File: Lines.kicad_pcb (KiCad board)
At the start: 2 copper layers, 29.5 x 100 mm, 0 parts

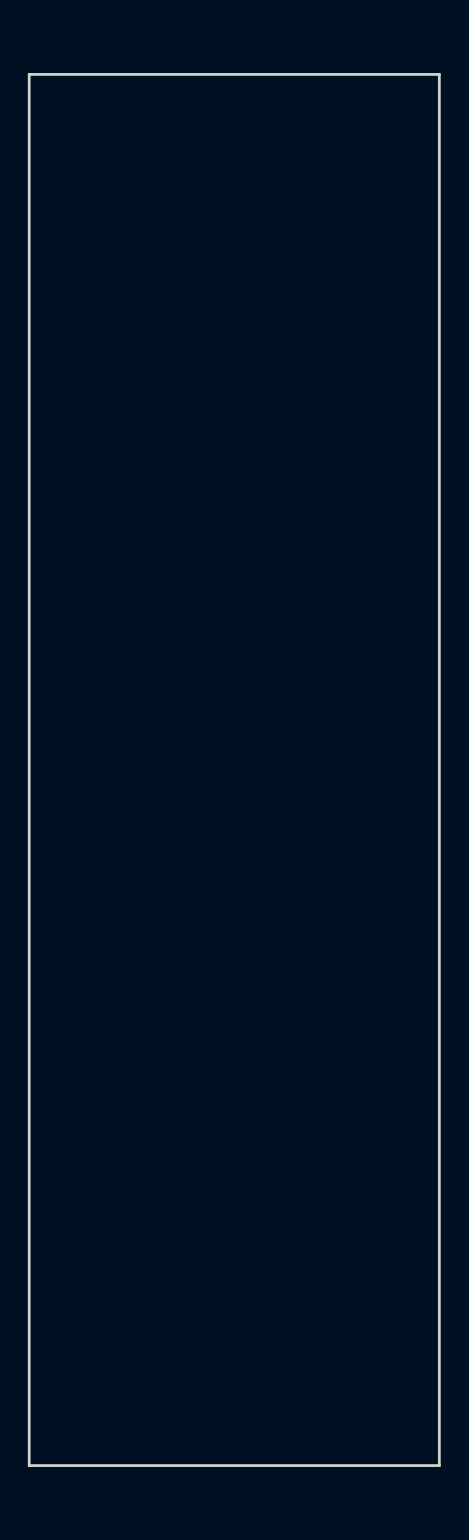
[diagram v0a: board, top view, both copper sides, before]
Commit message: Corrected board dimensions and added jacks.
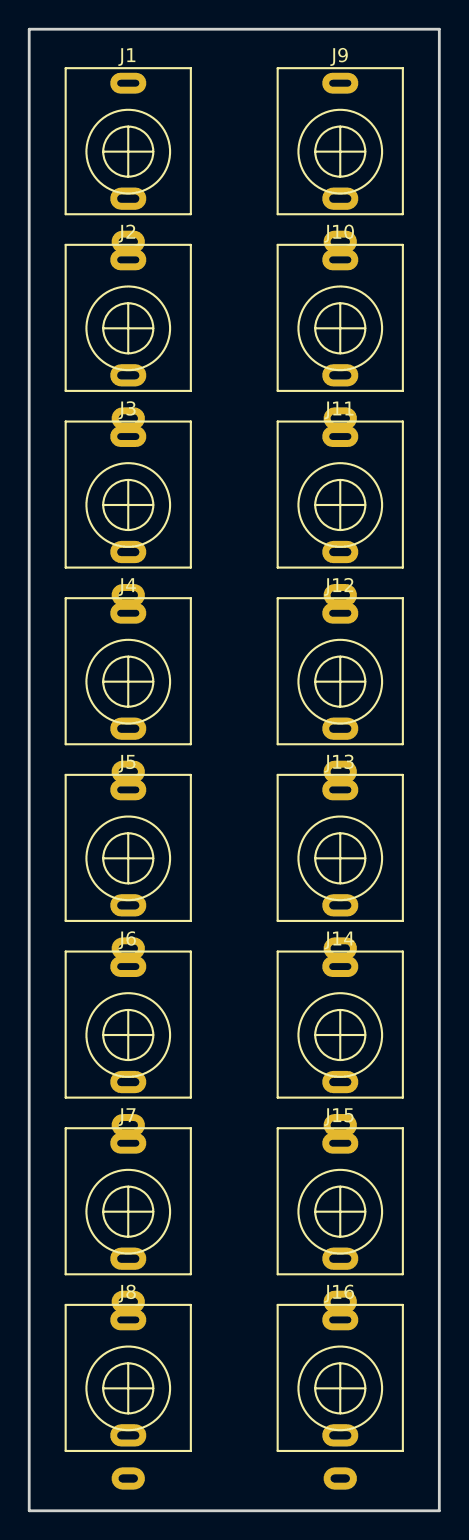
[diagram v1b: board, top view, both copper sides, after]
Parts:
- added J1: AudioJack2_SwitchT, Local:PJ398SM, F.Cu at (119.4, 57.1)
- added J10: AudioJack2_SwitchT, Local:PJ398SM, F.Cu at (134.6, 69.8)
- added J11: AudioJack2_SwitchT, Local:PJ398SM, F.Cu at (134.6, 82.5)
- added J12: AudioJack2_SwitchT, Local:PJ398SM, F.Cu at (134.6, 95.2)
- added J13: AudioJack2_SwitchT, Local:PJ398SM, F.Cu at (134.6, 108.0)
- added J14: AudioJack2_SwitchT, Local:PJ398SM, F.Cu at (134.6, 120.7)
- added J15: AudioJack2_SwitchT, Local:PJ398SM, F.Cu at (134.6, 133.3)
- added J16: AudioJack2_SwitchT, Local:PJ398SM, F.Cu at (134.6, 146.1)
- added J2: AudioJack2_SwitchT, Local:PJ398SM, F.Cu at (119.4, 69.8)
- added J3: AudioJack2_SwitchT, Local:PJ398SM, F.Cu at (119.4, 82.5)
- added J4: AudioJack2_SwitchT, Local:PJ398SM, F.Cu at (119.4, 95.2)
- added J5: AudioJack2_SwitchT, Local:PJ398SM, F.Cu at (119.4, 108.0)
- added J6: AudioJack2_SwitchT, Local:PJ398SM, F.Cu at (119.4, 120.7)
- added J7: AudioJack2_SwitchT, Local:PJ398SM, F.Cu at (119.4, 133.3)
- added J8: AudioJack2_SwitchT, Local:PJ398SM, F.Cu at (119.4, 146.1)
- added J9: AudioJack2_SwitchT, Local:PJ398SM, F.Cu at (134.6, 57.1)
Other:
- board size 29.5 x 100 mm -> 29.5 x 106.5 mm

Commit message: Complete placement.
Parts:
- added C1: 220p, Capacitor_SMD:C_0603_1608Metric, B.Cu at (125.0, 86.2)
- added C10: 100n, Capacitor_SMD:C_0603_1608Metric, B.Cu at (122.0, 133.3)
- added C11: 220p, Capacitor_SMD:C_0603_1608Metric, B.Cu at (129.2, 142.4)
- added C12: 220p, Capacitor_SMD:C_0603_1608Metric, B.Cu at (125.0, 142.4)
- added C13: 22u, Capacitor_SMD:CP_Elec_5x5.4, B.Cu at (119.4, 70.6)
- added C14: 22u, Capacitor_SMD:CP_Elec_5x5.4, B.Cu at (134.9, 70.6)
- added C2: 220p, Capacitor_SMD:C_0603_1608Metric, B.Cu at (129.2, 86.2)
- added C3: 100n, Capacitor_SMD:C_0603_1608Metric, B.Cu at (122.0, 95.2)
- added C4: 100n, Capacitor_SMD:C_0603_1608Metric, B.Cu at (132.0, 95.2)
- added C5: 220p, Capacitor_SMD:C_0603_1608Metric, B.Cu at (129.2, 104.3)
- added C6: 220p, Capacitor_SMD:C_0603_1608Metric, B.Cu at (125.0, 104.3)
- added C7: 220p, Capacitor_SMD:C_0603_1608Metric, B.Cu at (125.0, 124.3)
- added C8: 220p, Capacitor_SMD:C_0603_1608Metric, B.Cu at (129.2, 124.3)
- added C9: 100n, Capacitor_SMD:C_0603_1608Metric, B.Cu at (132.0, 133.3)
- added D1: DFLR1400-7, Diode_SMD:D_PowerDI-123, B.Cu at (115.4, 59.8)
- added D2: DFLR1400-7, Diode_SMD:D_PowerDI-123, B.Cu at (138.8, 59.8)
- added D3: LED, LED_SMD:LED_0603_1608Metric_Castellated, B.Cu at (115.4, 52.8)
- added FB1: Ferrite_Bead, Inductor_SMD:L_0603_1608Metric, B.Cu at (115.4, 65.0)
- added FB2: Ferrite_Bead, Inductor_SMD:L_0603_1608Metric, B.Cu at (138.8, 65.0)
- added J17: Conn_02x05_Odd_Even, Connector_PinHeader_2.54mm:PinHeader_2x05_P2.54mm_Vertical, B.Cu at (125.7, 62.6)
- added R1: 100k, Resistor_SMD:R_0603_1608Metric, B.Cu at (119.4, 56.3)
- added R10: 680, Resistor_SMD:R_0603_1608Metric, B.Cu at (129.2, 77.5)
- added R11: 100k, Resistor_SMD:R_0603_1608Metric, B.Cu at (119.4, 81.5)
- added R12: 100k, Resistor_SMD:R_0603_1608Metric, B.Cu at (119.4, 96.3)
- added R13: 47k, Resistor_SMD:R_0603_1608Metric, B.Cu at (129.2, 110.1)
- added R14: 47k, Resistor_SMD:R_0603_1608Metric, B.Cu at (125.0, 110.1)
- added R15: 33k, Resistor_SMD:R_0603_1608Metric, B.Cu at (129.2, 107.2)
- added R16: 33k, Resistor_SMD:R_0603_1608Metric, B.Cu at (125.0, 107.2)
- added R17: 33k, Resistor_SMD:R_0603_1608Metric, B.Cu at (129.2, 101.3)
- added R18: 33k, Resistor_SMD:R_0603_1608Metric, B.Cu at (125.0, 101.3)
- added R19: 680, Resistor_SMD:R_0603_1608Metric, B.Cu at (134.6, 81.5)
- added R2: 100k, Resistor_SMD:R_0603_1608Metric, B.Cu at (125.0, 77.5)
- added R20: 680, Resistor_SMD:R_0603_1608Metric, B.Cu at (134.6, 96.3)
- added R21: 100k, Resistor_SMD:R_0603_1608Metric, B.Cu at (119.4, 107.0)
- added R22: 100k, Resistor_SMD:R_0603_1608Metric, B.Cu at (119.4, 121.6)
- added R23: 47k, Resistor_SMD:R_0603_1608Metric, B.Cu at (125.0, 118.5)
- added R24: 47k, Resistor_SMD:R_0603_1608Metric, B.Cu at (129.2, 118.5)
- added R25: 33k, Resistor_SMD:R_0603_1608Metric, B.Cu at (125.0, 121.4)
- added R26: 33k, Resistor_SMD:R_0603_1608Metric, B.Cu at (129.2, 121.4)
- added R27: 33k, Resistor_SMD:R_0603_1608Metric, B.Cu at (125.0, 127.3)
- added R28: 33k, Resistor_SMD:R_0603_1608Metric, B.Cu at (129.2, 127.3)
- added R29: 680, Resistor_SMD:R_0603_1608Metric, B.Cu at (134.6, 107.0)
- added R3: 47k, Resistor_SMD:R_0603_1608Metric, B.Cu at (125.0, 80.4)
- added R30: 680, Resistor_SMD:R_0603_1608Metric, B.Cu at (134.6, 121.6)
- added R31: 100k, Resistor_SMD:R_0603_1608Metric, B.Cu at (119.4, 132.4)
- added R32: 100k, Resistor_SMD:R_0603_1608Metric, B.Cu at (119.4, 147.0)
- added R33: 47k, Resistor_SMD:R_0603_1608Metric, B.Cu at (129.2, 148.2)
- added R34: 47k, Resistor_SMD:R_0603_1608Metric, B.Cu at (125.0, 148.2)
- added R35: 33k, Resistor_SMD:R_0603_1608Metric, B.Cu at (129.2, 145.3)
- added R36: 33k, Resistor_SMD:R_0603_1608Metric, B.Cu at (125.0, 145.3)
- added R37: 33k, Resistor_SMD:R_0603_1608Metric, B.Cu at (129.2, 139.4)
- added R38: 33k, Resistor_SMD:R_0603_1608Metric, B.Cu at (125.0, 139.4)
- added R39: 680, Resistor_SMD:R_0603_1608Metric, B.Cu at (134.6, 132.4)
- added R4: 47k, Resistor_SMD:R_0603_1608Metric, B.Cu at (129.2, 80.4)
- added R40: 680, Resistor_SMD:R_0603_1608Metric, B.Cu at (134.6, 147.0)
- added R41: 1k, Resistor_SMD:R_0603_1608Metric, B.Cu at (138.8, 52.6)
- added R5: 33k, Resistor_SMD:R_0603_1608Metric, B.Cu at (125.0, 83.3)
- added R6: 33k, Resistor_SMD:R_0603_1608Metric, B.Cu at (129.2, 83.3)
- added R7: 33k, Resistor_SMD:R_0603_1608Metric, B.Cu at (125.0, 89.2)
- added R8: 33k, Resistor_SMD:R_0603_1608Metric, B.Cu at (129.2, 89.2)
- added R9: 680, Resistor_SMD:R_0603_1608Metric, B.Cu at (134.6, 56.3)
- added U1: TL074, Package_SO:TSSOP-14_4.4x5mm_P0.65mm, B.Cu at (127.0, 95.2)
- added U2: TL074, Package_SO:TSSOP-14_4.4x5mm_P0.65mm, B.Cu at (127.0, 133.3)
- turned J10 to 180 degrees
- turned J12 to 180 degrees
- turned J14 to 180 degrees
- turned J16 to 180 degrees
- turned J2 to 180 degrees
- turned J4 to 180 degrees
- turned J6 to 180 degrees
- turned J8 to 180 degrees
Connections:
- J1 pad T: Net-(J1-PadT) -> IN1
- J10 pad T: Net-(J10-PadT) -> OUT2
- J11 pad T: Net-(J11-PadT) -> OUT3
- J12 pad T: Net-(J12-PadT) -> OUT4
- J13 pad T: Net-(J13-PadT) -> OUT5
- J14 pad T: Net-(J14-PadT) -> OUT6
- J15 pad T: Net-(J15-PadT) -> OUT7
- J16 pad T: Net-(J16-PadT) -> OUT8
- J2 pad T: Net-(J2-PadT) -> IN2
- J3 pad T: Net-(J3-PadT) -> IN3
- J4 pad T: Net-(J4-PadT) -> IN4
- J5 pad T: Net-(J5-PadT) -> IN5
- J6 pad T: Net-(J6-PadT) -> IN6
- J7 pad T: Net-(J7-PadT) -> IN7
- J8 pad T: Net-(J8-PadT) -> IN8
- J9 pad T: Net-(J9-PadT) -> OUT1

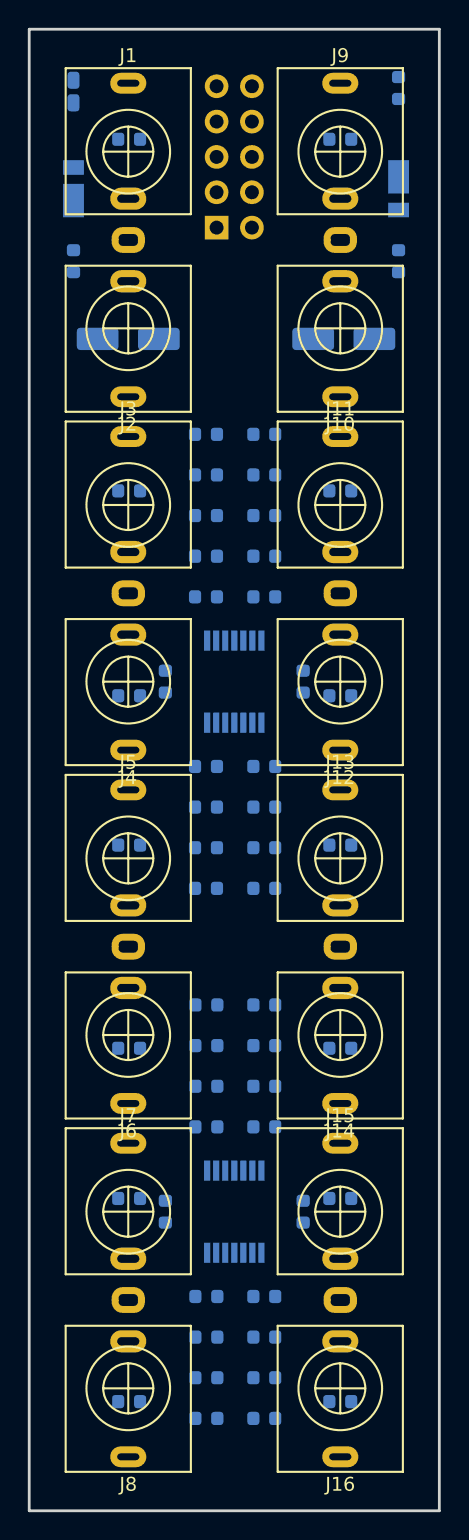
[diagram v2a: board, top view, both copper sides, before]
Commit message: Hand-routed power rails.
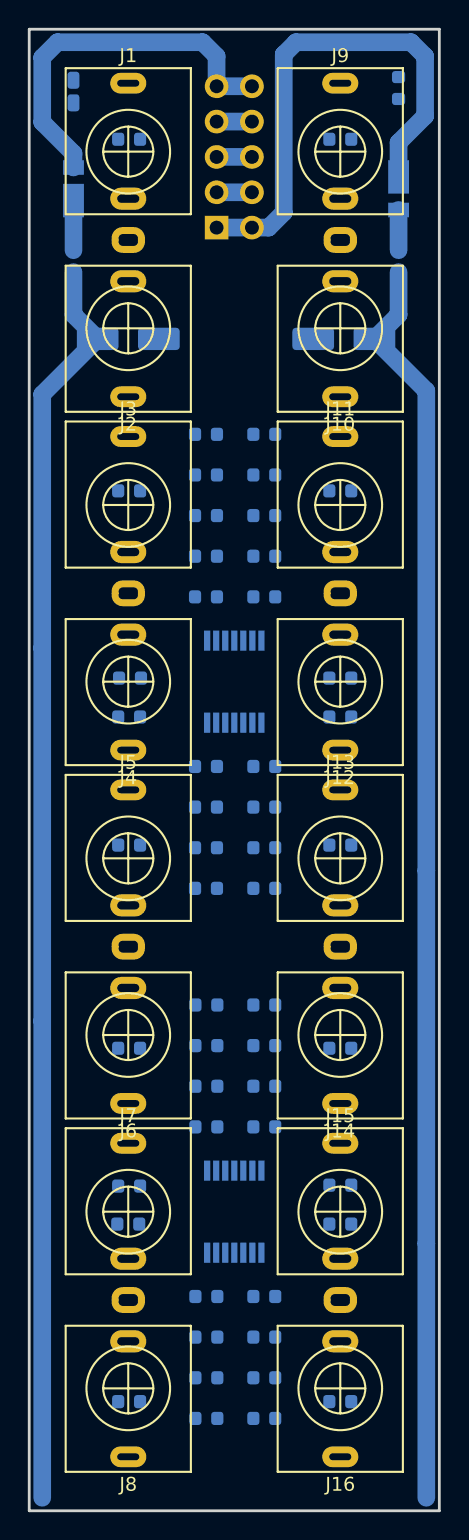
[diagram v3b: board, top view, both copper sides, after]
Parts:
- moved C9 3.28 mm to (134.6, 131.4), turned to 0 degrees
- moved C10 2.81 mm to (119.4, 134.2), turned to 0 degrees
- moved C4 2.68 mm to (134.6, 95.0), turned to 180 degrees
- moved C3 2.55 mm to (119.5, 95.0), turned to 180 degrees
- moved R39 1.84 mm to (134.6, 134.2)
- moved R12 1.52 mm to (119.4, 97.8)
- moved R20 1.52 mm to (134.6, 97.8)
- moved R31 0.89 mm to (119.4, 131.5)
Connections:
- C10 pad 1: GND -> (no net)
- C13 pad 2: GND -> (no net)
- C14 pad 1: GND -> (no net)
- C3 pad 2: GND -> (no net)
- C4 pad 1: GND -> (no net)
- C9 pad 2: GND -> (no net)
- D3 pad 2: GND -> (no net)
- J1 pad S: GND -> (no net)
- J1 pad TN: GND -> (no net)
- J10 pad S: GND -> (no net)
- J11 pad S: GND -> (no net)
- J12 pad S: GND -> (no net)
- J13 pad S: GND -> (no net)
- J14 pad S: GND -> (no net)
- J15 pad S: GND -> (no net)
- J16 pad S: GND -> (no net)
- J17 pad 3: GND -> (no net)
- J17 pad 4: GND -> (no net)
- J17 pad 5: GND -> (no net)
- J17 pad 6: GND -> (no net)
- J17 pad 7: GND -> (no net)
- J17 pad 8: GND -> (no net)
- J2 pad S: GND -> (no net)
- J2 pad TN: GND -> (no net)
- J3 pad S: GND -> (no net)
- J3 pad TN: GND -> (no net)
- J4 pad S: GND -> (no net)
- J4 pad TN: GND -> (no net)
- J5 pad S: GND -> (no net)
- J5 pad TN: GND -> (no net)
- J6 pad S: GND -> (no net)
- J6 pad TN: GND -> (no net)
- J7 pad S: GND -> (no net)
- J7 pad TN: GND -> (no net)
- J8 pad S: GND -> (no net)
- J8 pad TN: GND -> (no net)
- J9 pad S: GND -> (no net)
- R13 pad 2: GND -> (no net)
- R14 pad 2: GND -> (no net)
- R15 pad 1: GND -> (no net)
- R16 pad 1: GND -> (no net)
- R23 pad 2: GND -> (no net)
- R24 pad 2: GND -> (no net)
- R25 pad 1: GND -> (no net)
- R26 pad 1: GND -> (no net)
- R3 pad 2: GND -> (no net)
- R33 pad 2: GND -> (no net)
- R34 pad 2: GND -> (no net)
- R35 pad 1: GND -> (no net)
- R36 pad 1: GND -> (no net)
- R4 pad 2: GND -> (no net)
- R5 pad 1: GND -> (no net)
- R6 pad 1: GND -> (no net)
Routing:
- net +12V: track 0.00 -> 90.5 mm
- net -12V: track 0.00 -> 90.4 mm
- net Net-(D2-Pad1): track 0.00 -> 37.0 mm
- net Net-(D1-Pad2): track 0.00 -> 26.9 mm
- net (no net): track 0.00 -> 7.62 mm
- net Net-(D1-Pad1): track 0.00 -> 3.57 mm
- net Net-(D2-Pad2): track 0.00 -> 2.89 mm
